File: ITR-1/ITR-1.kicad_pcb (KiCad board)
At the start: 2 copper layers, 30 x 45 mm, 50 parts, among them K1 Кнопка_KLS7-TS5401-1.35-250-T, K2 Кнопка_KLS7-TS5401-1.35-250-T, X1 отверстие_под_пайку, X2 отверстие_под_пайку

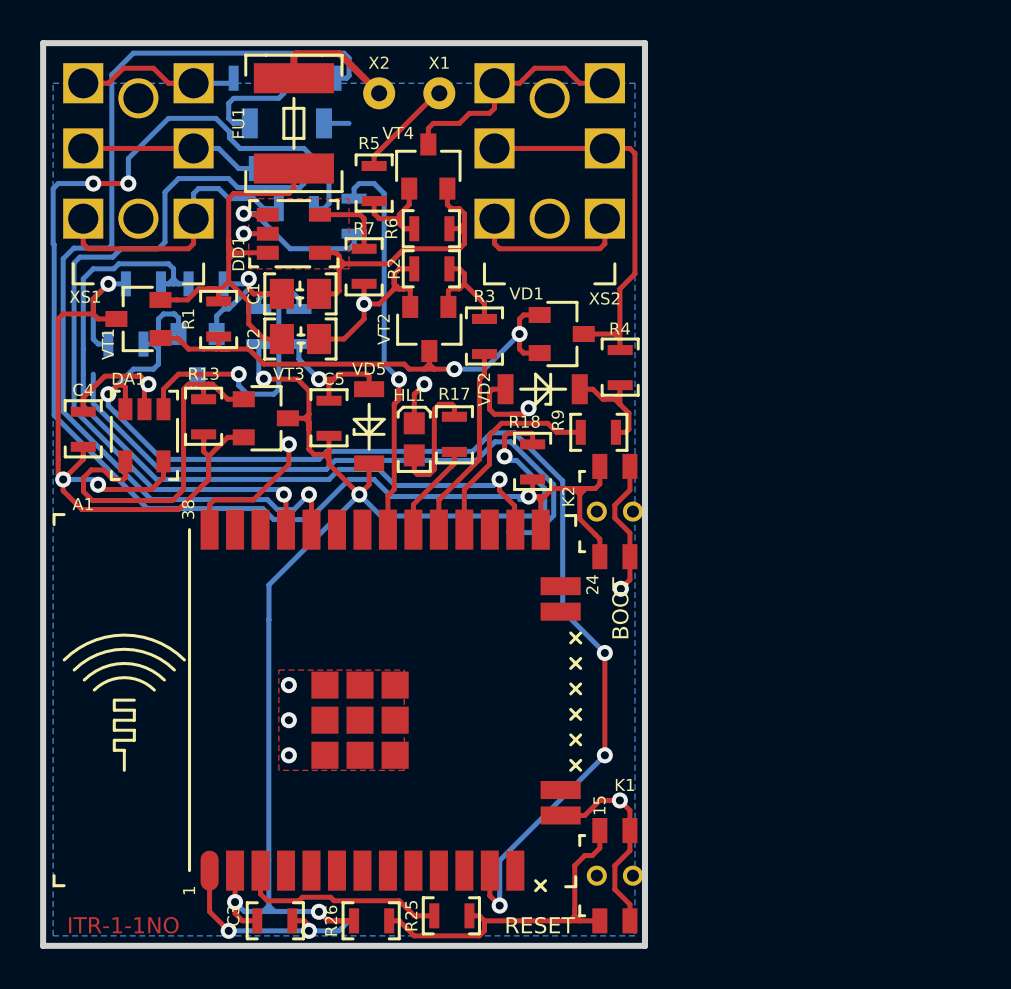
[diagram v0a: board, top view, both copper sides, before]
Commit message: аналоговые каналы перенесены на ADC1
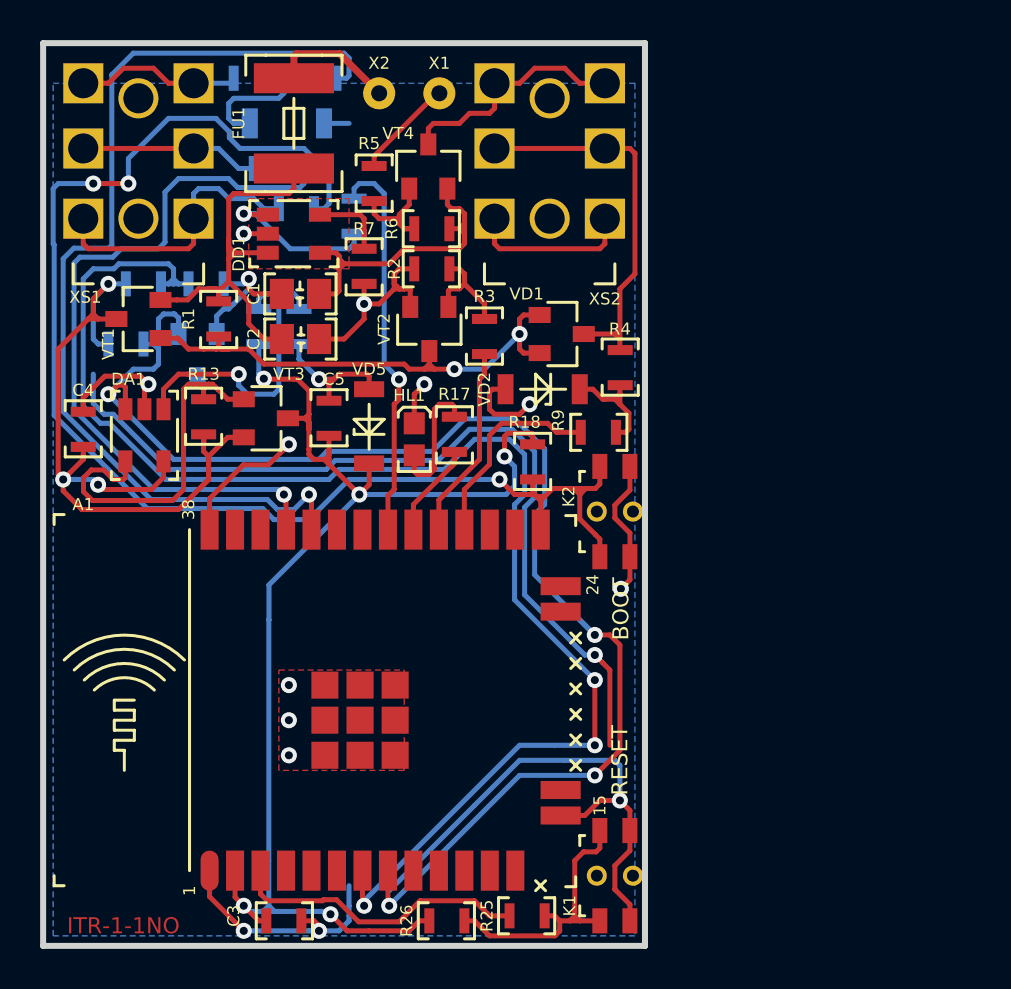
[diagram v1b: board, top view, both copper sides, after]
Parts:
- moved R25 3.75 mm to (124.1, 98.5)
- moved R26 3.75 mm to (120.1, 98.8)
- moved C3 0.45 mm to (112.0, 98.8)
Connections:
- A1 pad 12: /AN.2V5.REF -> Net-(A1-Pad12)
- A1 pad 26: /AN.BAT.MEASURE -> Net-(A1-Pad26)
- A1 pad 7: Net-(A1-Pad7) -> /AN.BAT.MEASURE
- A1 pad 8: Net-(A1-Pad8) -> /AN.2V5.REF
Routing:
- net /AN.BAT.MEASURE: track 39.8 -> 71.9 mm, vias 1 -> 3
- net /GND: track 119.9 -> 147.9 mm, vias 15 -> 16
- net /AN.2V5.REF: track 62.8 -> 71.0 mm
- net /RESET: track 10.4 -> 14.9 mm
- net Net-(K1-Pad1): track 18.0 -> 14.4 mm

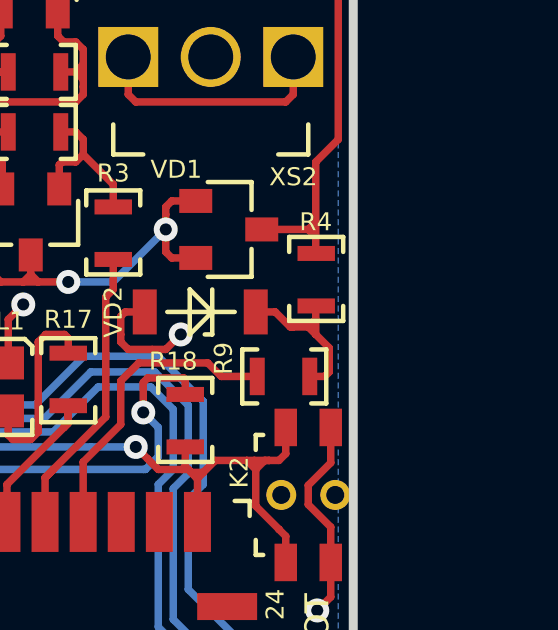
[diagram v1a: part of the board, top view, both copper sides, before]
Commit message: изменено опорное + подключение к мотору; заготовка под 2 светодиода
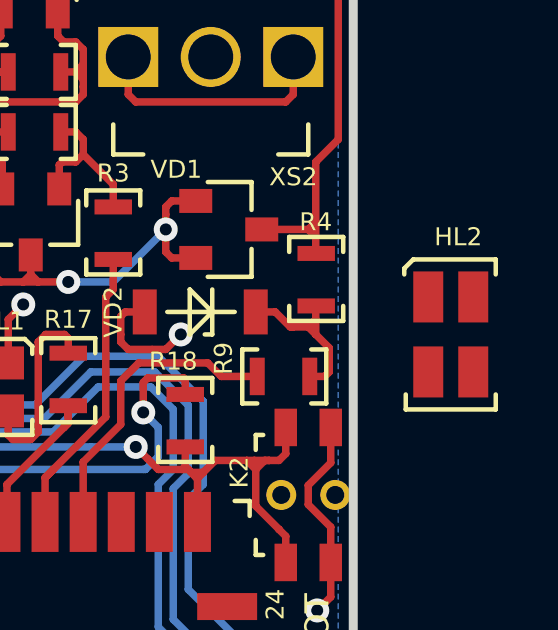
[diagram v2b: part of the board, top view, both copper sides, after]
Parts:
- added HL2: Светодиод_сдвоенный_KPB-3025SURKCGKC, N_VD_HL:Светодиод_SMD_m3025, F.Cu at (132.5, 71.8)
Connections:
- net Net-(DA1-Pad1) renamed /U.FB

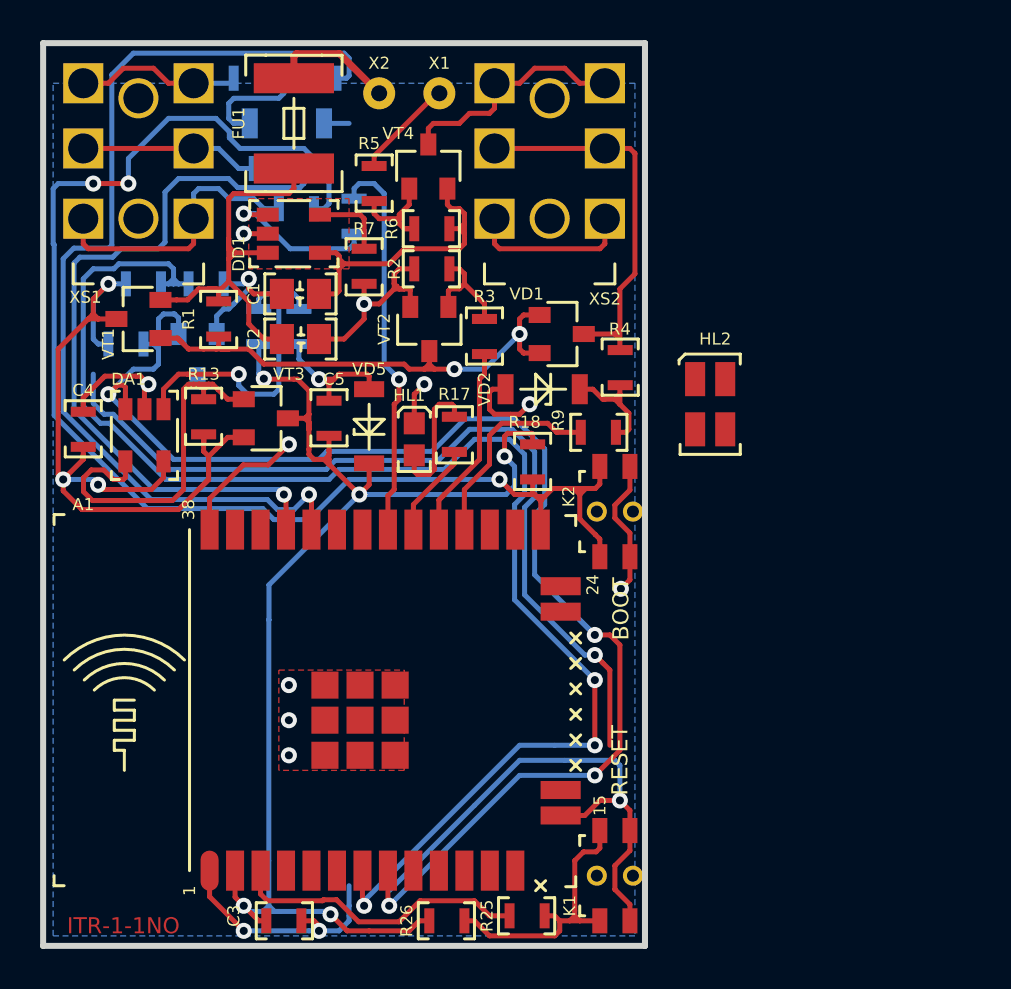
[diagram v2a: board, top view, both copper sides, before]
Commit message: модифицирована тайминги обмена с сервером, LED заменен на 2хцветный
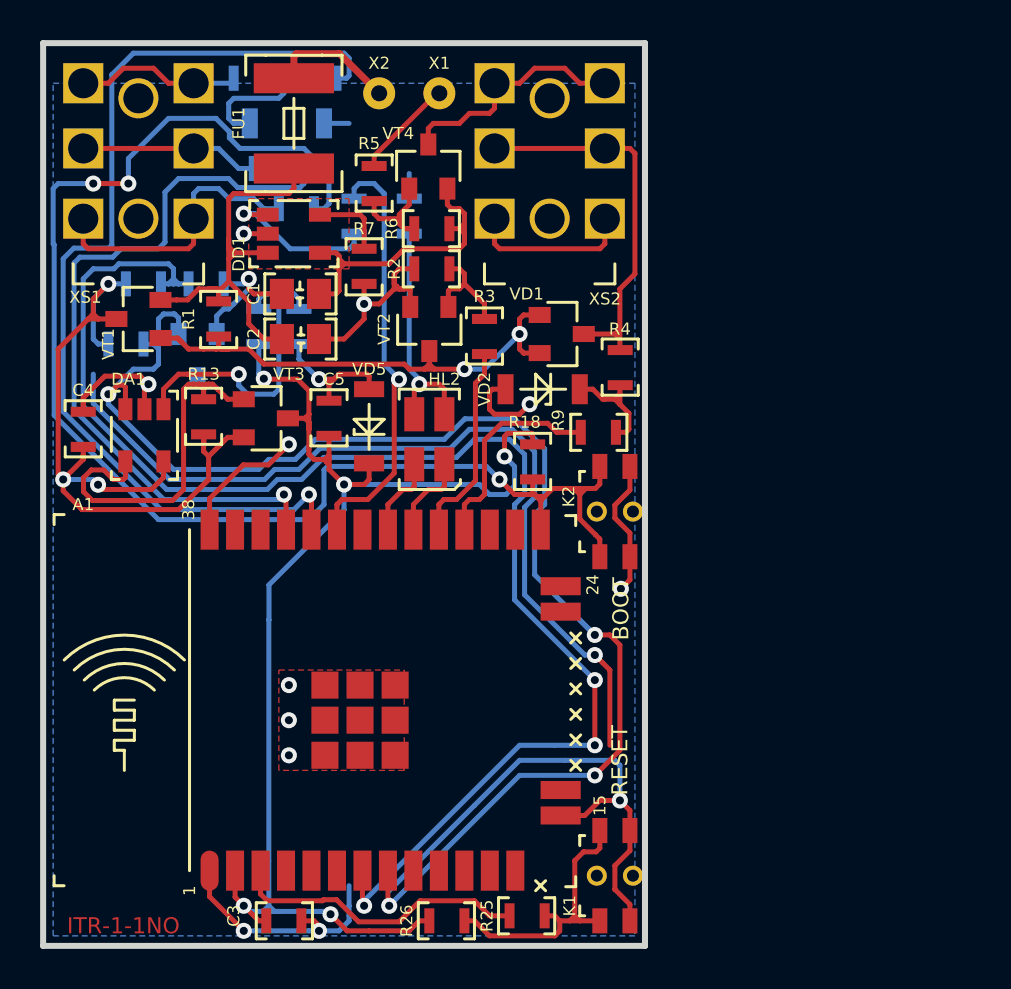
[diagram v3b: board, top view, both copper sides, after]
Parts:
- removed HL1: Светодиод, N_VD_HL:Светодиод_SMD_IEC_0603
- R17: moved to B.Cu
- moved HL2 13.2 mm to (120.0, 76.0), turned to 180 degrees
- moved R17 11.1 mm to (118.2, 63.6)
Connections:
- A1 pad 30: /LED -> /LED1
- A1 pad 31: /CHARGE.MODE -> /LED2
- A1 pad 33: Net-(A1-Pad33) -> /CHARGE.MODE
- HL2 pad 1: Net-(HL2-Pad1) -> /LED1
- HL2 pad 3: Net-(HL2-Pad3) -> /LED2
- HL2 pad 4: Net-(HL2-Pad4) -> Net-(HL2-Pad2)
- R17 pad 1: Net-(HL1-PadA) -> /GND
- R17 pad 2: /LED -> Net-(HL2-Pad2)
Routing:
- net Net-(HL2-Pad2): track 0.00 -> 11.9 mm, vias 0 -> 1
- net Net-(HL1-PadA): track 6.62 -> 0.00 mm
- net /LED: track 5.05 -> 0.00 mm
- net /LED1: track 0.00 -> 4.27 mm
- net /LED2: track 0.00 -> 4.04 mm
- net /CHARGE.MODE: track 19.6 -> 21.4 mm
- net /BOOT: track 70.4 -> 71.9 mm
- net /3V3: track 67.2 -> 68.1 mm
- net /AN.2V5.REF: track 71.0 -> 71.7 mm
- net /GND: track 147.9 -> 147.4 mm, vias 16 -> 15

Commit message: зарядка через USB, в сервисный джек добавлена земля, кнопка впаивается
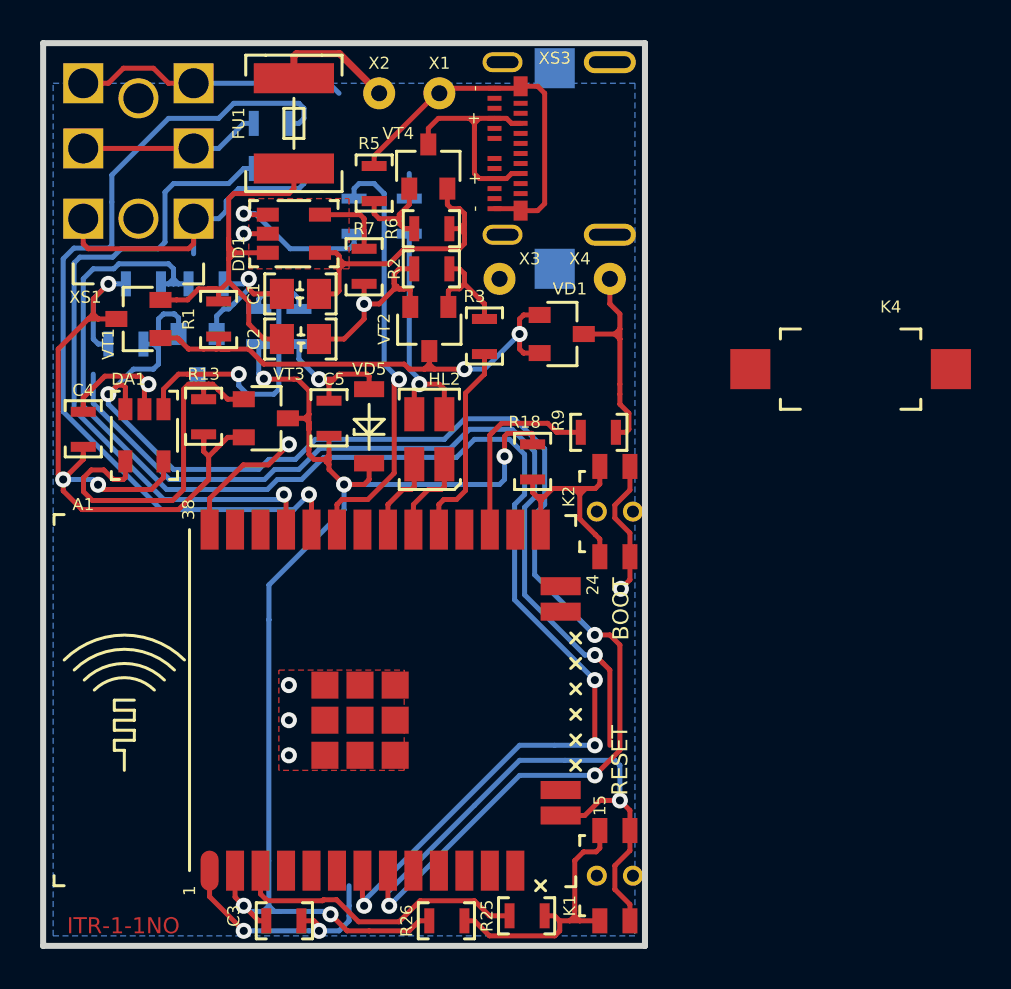
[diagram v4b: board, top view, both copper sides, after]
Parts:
- removed R21, R22, R4: Резистор_0,065Вт, N_RLC:Резистор_SMD_0603_0,065_Вт
- removed VD2: Стабилитрон_BZV55-C3V9, N_VD_HL:SOD-80
- removed VD4: Стабилитрон_BZV55C2V7, N_VD_HL:SOD-80
- removed XS2: Клеммник_х3, N_X:jack_ST-033
- added K3: кнопка, N_X:Кнопка_FSMSM, B.Cu at (125.5, 66.2)
- added K4: кнопка, N_X:Кнопка_FSMSM, F.Cu at (135.2, 71.2)
- added X3: отверстие_под_пайку, N_X:ОтверстиеD1.2, F.Cu at (122.8, 66.8)
- added X4: отверстие_под_пайку, N_X:ОтверстиеD1.2, F.Cu at (128.2, 66.8)
- added XS3: UBS-type-C-105450-0101&упрощенная, N_X:usb-type-c, F.Cu at (122.5, 63.2)
- moved R19 2.46 mm to (111.4, 59.0)
- turned R20 to 0 degrees
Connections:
- A1 pad 27: Net-(A1-Pad27) -> /BUTT.TURN
- A1 pad 28: /BUTT.TURN -> Net-(A1-Pad28)
- R19 pad 1: Net-(R19-Pad1) -> /UART.RX
- R9 pad 2: Net-(R4-Pad1) -> /EXT.BUTT
- XS1 pad 1: /OUT.RX -> /GND
- XS1 pad 2: /OUT.TX -> /OUT.RX
- XS1 pad 3: /OUT.BOOT -> /OUT.TX
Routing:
- net /BOOT: track 71.9 -> 12.3 mm, vias 3 -> 0
- net /OUT.BOOT: track 14.2 -> 0.00 mm
- net /GND: track 147.4 -> 161.2 mm, vias 15 -> 14
- net /OUT.TX: track 8.91 -> 17.8 mm
- net /EXT.BUTT: track 19.4 -> 10.8 mm
- net Net-(R19-Pad1): track 7.69 -> 0.00 mm
- net /UART.RX: track 49.1 -> 42.7 mm
- net Net-(R4-Pad1): track 5.81 -> 0.00 mm
- net /UART.TX: track 37.8 -> 33.9 mm
- net /3V3: track 68.1 -> 66.8 mm
- net /OUT.RX: track 8.12 -> 9.02 mm
- net /BUTT.TURN: track 10.5 -> 9.68 mm
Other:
- copper layers 2 -> 4
- board text removed: "BUTT"
- board text removed: "GND"
- board text removed: "UIN"

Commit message: ITR-1-1NN(45x30): +2 отв. под внеш. кнопки, -избыт. защита входов
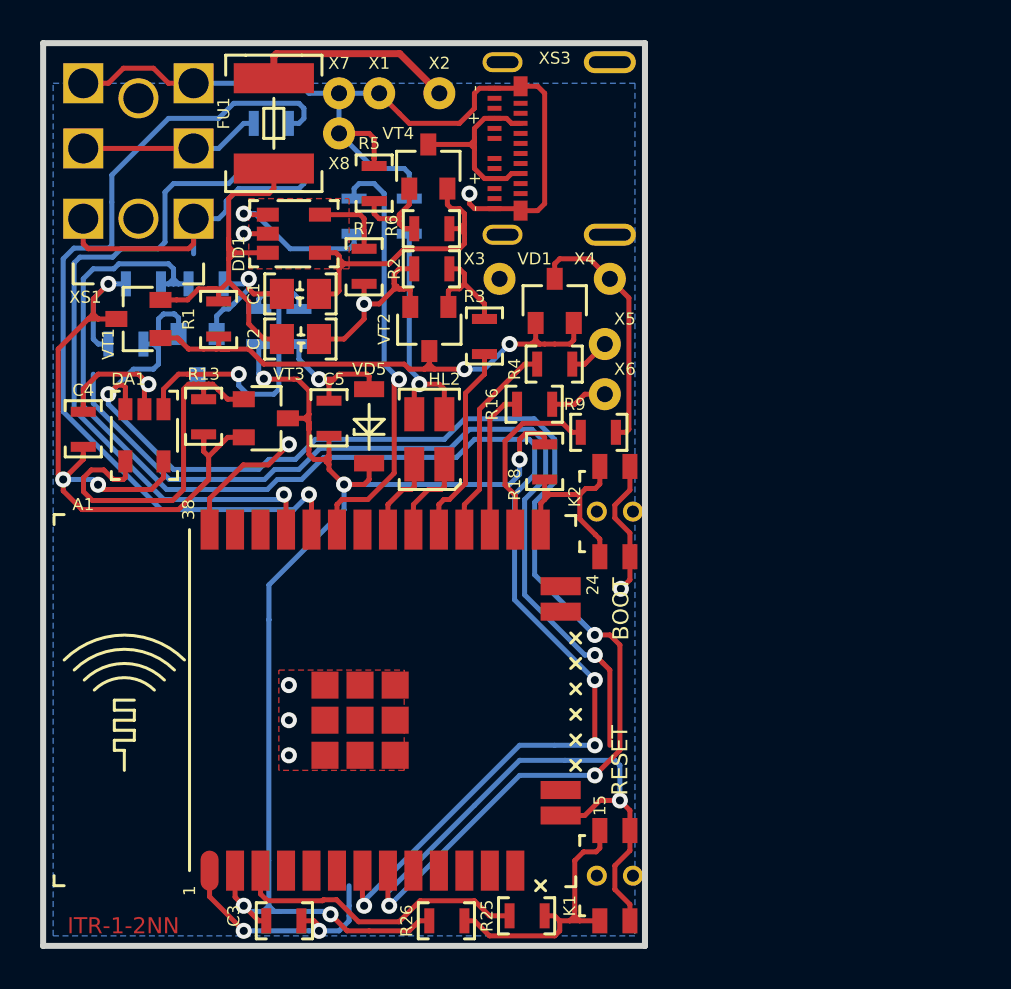
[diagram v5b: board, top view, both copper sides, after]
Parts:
- removed K3, K4: кнопка, N_X:Кнопка_FSMSM
- added R16: Резистор_0,065Вт, N_RLC:Резистор_SMD_0603_0,065_Вт, F.Cu at (124.5, 73.0)
- added R4: Резистор_0,065Вт, N_RLC:Резистор_SMD_0603_0,065_Вт, F.Cu at (125.5, 71.0)
- added X5: отверстие_под_пайку, N_X:ОтверстиеD1.2, F.Cu at (128.0, 70.0)
- added X6: отверстие_под_пайку, N_X:ОтверстиеD1.2, F.Cu at (128.0, 72.5)
- added X7: отверстие_под_пайку, N_X:ОтверстиеD1.2, F.Cu at (114.8, 57.5)
- added X8: отверстие_под_пайку, N_X:ОтверстиеD1.2, F.Cu at (114.8, 59.5)
- moved X1 3.00 mm to (116.8, 57.5)
- moved X2 3.00 mm to (119.8, 57.5)
- moved VD1 1.69 mm to (125.5, 67.8), turned to 90 degrees
- moved FU1 1.00 mm to (111.5, 56.8)
- moved R18 0.60 mm to (125.0, 75.9)
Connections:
- A1 pad 26: Net-(A1-Pad26) -> /BUTT.TURN
- A1 pad 27: /BUTT.TURN -> Net-(A1-Pad27)
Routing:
- net /GND: track 161.2 -> 175.8 mm, vias 14 -> 15
- net Net-(A1-Pad28): track 0.00 -> 10.1 mm
- net Net-(A1-Pad27): track 0.00 -> 7.18 mm
- net /BAT.IN: track 6.22 -> 10.7 mm
- net Net-(R16-Pad1): track 0.00 -> 2.83 mm
- net Net-(R4-Pad1): track 0.00 -> 2.04 mm
- net /BOOT: track 12.3 -> 10.4 mm
- net /U.IN: track 11.9 -> 9.99 mm
- net /EXT.BUTT: track 10.8 -> 12.6 mm
- net Net-(R1-Pad2): track 25.8 -> 26.9 mm
- net /BAT.CHARGE: track 21.5 -> 20.5 mm
- net /AN.BAT.MEASURE: track 72.3 -> 73.3 mm
- net /AN.2V5.REF: track 71.7 -> 72.7 mm
- net /BUTT.TURN: track 9.68 -> 8.95 mm
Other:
- copper layers 4 -> 2
- board text added: "BUT1"
- board text added: "BUT2"
- board text added: "EXT.BT"
- board text added: "GND"
- board text added: "ITR-1-2NN"
- board text removed: "ITR-1-1NO"
